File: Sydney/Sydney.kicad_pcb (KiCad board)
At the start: 2 copper layers, 54 x 87.6 mm, 5 parts, among them J1 Conn_01x02_Pin, U1 NT3H2111W0FHKH

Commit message: lots of stuff
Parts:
- added REF**: Lanyard hole, Taranium-libs:Lanyard hole, F.Cu at (169.4, 65.2)
- C1, D1, J1, R1, U1: moved to B.Cu
- moved J1 91.2 mm to (217.3, 87.9), turned to 180 degrees
- moved U1 38.9 mm to (189.8, 95.5), turned to 180 degrees
- moved C1 36.6 mm to (187.0, 95.1), turned to -90 degrees
- moved R1 34.4 mm to (183.2, 93.7), turned to 180 degrees
- moved D1 32.4 mm to (183.0, 96.1), turned to 180 degrees
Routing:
- net Net-(J1-Pin_2): track 0.00 -> 51.3 mm, vias 0 -> 2
- net Net-(J1-Pin_1): track 0.00 -> 48.4 mm
- net Net-(D1-K): track 0.00 -> 9.92 mm
- net Net-(U1-VCC): track 0.00 -> 6.03 mm
- net Net-(D1-A): track 0.00 -> 2.53 mm
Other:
- board size 54 x 87.6 mm -> 99.1 x 54 mm

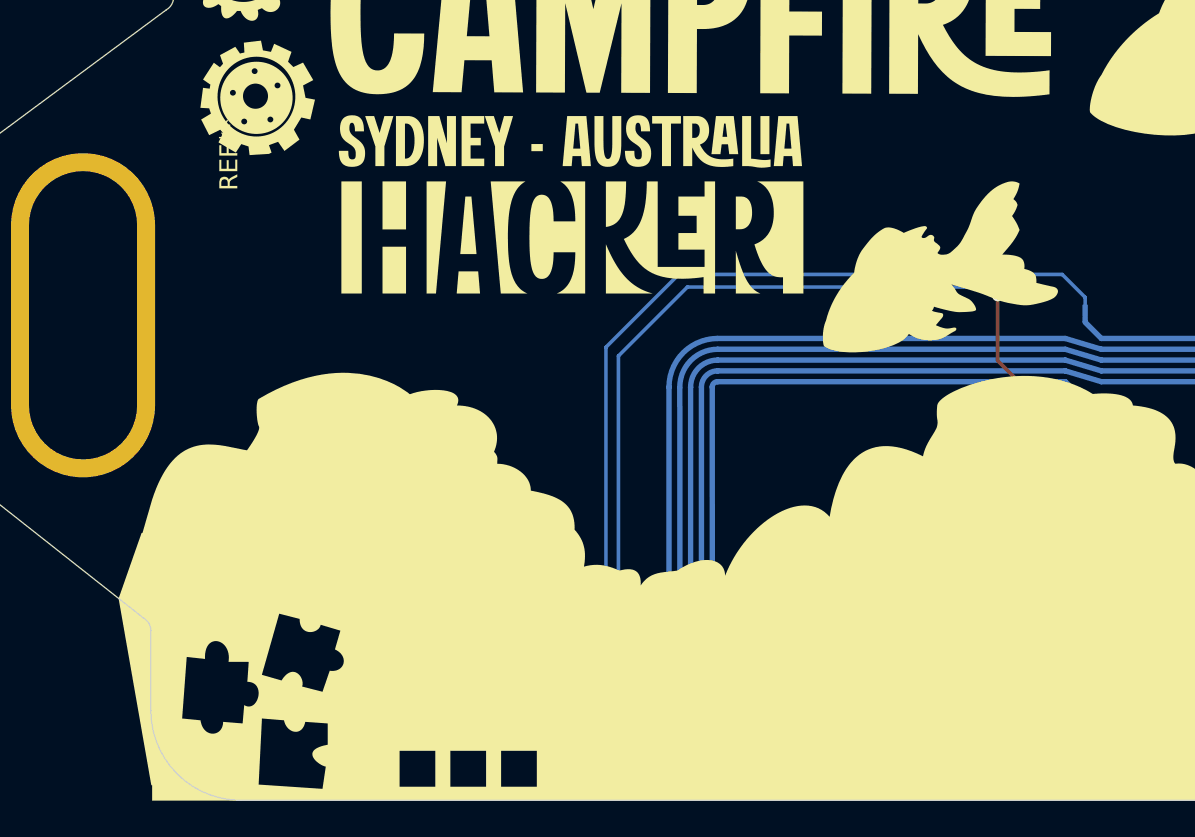
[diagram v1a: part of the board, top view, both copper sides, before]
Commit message: me want to die
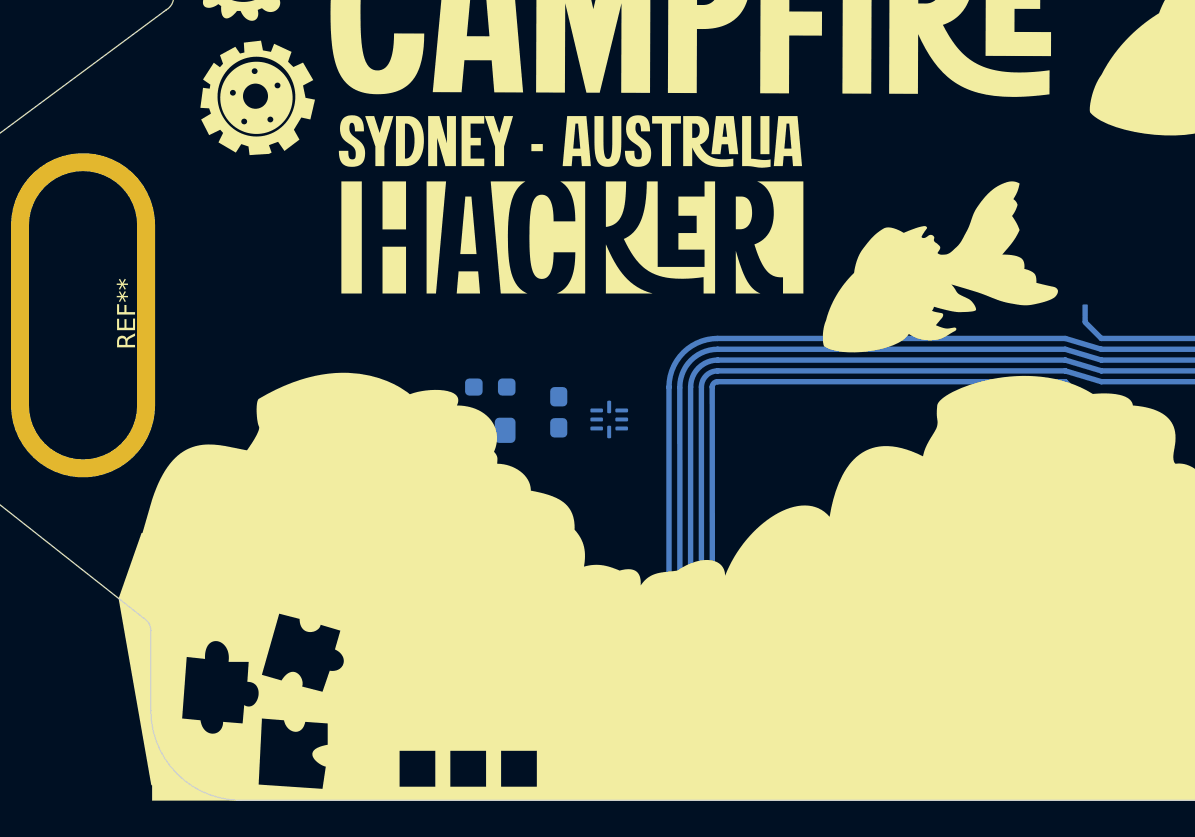
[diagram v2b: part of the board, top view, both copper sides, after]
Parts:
- moved C1 15.7 mm to (187.2, 79.5)
- moved D1 15.7 mm to (183.2, 80.5)
- moved R1 15.7 mm to (183.4, 78.1)
- moved U1 15.7 mm to (190.0, 79.9)
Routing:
- net Net-(J1-Pin_2): track 51.3 -> 0.00 mm, vias 2 -> 0
- net Net-(J1-Pin_1): track 48.4 -> 0.00 mm
- net Net-(D1-K): track 9.92 -> 0.00 mm
- net Net-(U1-VCC): track 6.03 -> 0.00 mm
- net Net-(D1-A): track 2.53 -> 0.00 mm

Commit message: finally works ish
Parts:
- moved C1 17.7 mm to (197.0, 94.2)
- moved D1 17.7 mm to (193.0, 95.2)
- moved U1 17.7 mm to (199.8, 94.6)
- moved R1 17.7 mm to (193.2, 92.8)
- moved J1 11.0 mm to (228.3, 87.7)
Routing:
- net Net-(J1-Pin_1): track 0.00 -> 47.5 mm
- net Net-(J1-Pin_2): track 0.00 -> 42.6 mm, vias 0 -> 2
- net Net-(D1-K): track 0.00 -> 9.60 mm
- net Net-(U1-VCC): track 0.00 -> 6.13 mm
- net Net-(D1-A): track 0.00 -> 2.53 mm
- added copper zone on B.Cu, net (none)
- added copper zone on F.Cu, net (none)
